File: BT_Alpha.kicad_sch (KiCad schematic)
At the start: 97 parts, among them J1 61300511121, J2 S6B-PH-K-S, J3 S6B-PH-K-S, J4 Boxed_Header_02x03_SMT, K1 AGQ200A12Z, M1 Mounting_Hole_2.7mm_Unplated, M2 Mounting_Hole_2.7mm_Unplated, M3 Mounting_Hole_2.7mm_Unplated, Q1 BSS123, Q2 BSS123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

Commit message: started iterating to rev. B
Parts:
- removed C16: 100nF, NRD_CAP:C_0603, symbol NRD_C_0603:CL10B104KB8NNNC
- removed C8, C9: 3.3nF, NRD_CAP:C_0603, symbol NRD_C_0603:CL10B332MB8NNNC
- removed J1: 61300511121, NRD_PinHeader:61300511121, symbol NRD_PinHeader:61300511121
- removed R1, R4: 470R, NRD_RES:R_0603, symbol NRD_R_0603:RC0603FR-07470RL
- removed R10, R11, R12, R22, R23, R24, R25, R27, R28, R29, R30, R9: 1M, NRD_RES:R_0603, symbol NRD_R_0603:RC0603FR-071ML
- removed R13, R14, R15: 0R, NRD_RES:R_0603, symbol NRD_R_0603:RC0603FR-070RL
- removed R16, R21, R26: 10K, NRD_RES:R_0603, symbol NRD_R_0603:RC0603FR-0710KL
- removed R33: 10K, NRD_R_Var:TC33X-2, symbol NRD_R_Var:TC33X-2-103E
- removed U3: TLV4888DR, NRD_IC_OPAMP:TLV4888DR, symbol NRD_IC_OPAMP:TLV4888DR
- removed Y1: XO32, Oscillator:Oscillator_SMD_EuroQuartz_XO32-4Pin_3.2x2.5mm, symbol Oscillator:XO32
- added C22, C37: 10uF, NRD_CAP:C_0805, symbol NRD_C_0805:CL21B106KOQNNNG
- added R41, R42, R43, R44: 10K, NRD_RES:R_0603, symbol NRD_R_0603:RC0603FR-0710KL
- added U3: TLV2888DR, NRD_IC_OPAMP:TLV2888DR, symbol NRD_IC_OPAMP:TLV2888DR
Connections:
- net SCK is gone; now on net ESP_IO0: U1.12 (SCK)
- net +12V: now also K1.8; no longer K1.1
- net GND: now also R41.1, R42.1, U3.4 (V-)
- net OUT_L: now also C22.2
- net OUT_R: now also C37.2
- net at C15.2, TP3.1: now also U3.6 (-), U3.7
- net at C14.2, TP2.1: now also U3.1, U3.2 (-)
- net at D1.A, Q1.3 (D): now also K1.1; no longer K1.8
- net +6V_FLT: now reaches C27.1, C36.1, L2.2
- net +6V_FLT: now also R43.2, R44.2, U3.8 (V+)
- net MCLK: no longer names the net of U2.27 (IO16)
- new net: C37.1, R41.2, R43.1, U3.5 (+)
- new net: C22.1, R42.2, R44.1, U3.3 (+)
- no-connect marks 27 -> 25
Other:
- note added: "(MCLK)"
- note added: "TLV2888"
- note removed: "(CLK_OUT1)"
- note removed: "(from MCU)"
- note removed: "(to DAC)"
- note removed: "AppNote uses 2.2nF for reconstruction filter. 2.2nF only as C0G in databbase -> 3.3nF C7R acceptable as well -> fg = 102.6kHz (instead of 153.9kHz)"
- note removed: "DAC Clock"
- note removed: "credits amplifier: https://electronics.stackexchange.com/questions/450609/op-amp-circuit-to-control-gain-of-two-analog-channels-with-one-single-section-po"
- moved on the sheet: C14, C15, D1, K1, Q1, Q2, R34, R8, TP2, TP3

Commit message: wip
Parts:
- removed TP1, TP2, TP3: 5001, NRD_MISC:500x, symbol NRD_MISC:5001
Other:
- moved on the sheet: M1, M2, M3

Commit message: added credits
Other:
- moved on the sheet: C14, C15, C34, Q2, R34, R39, R8

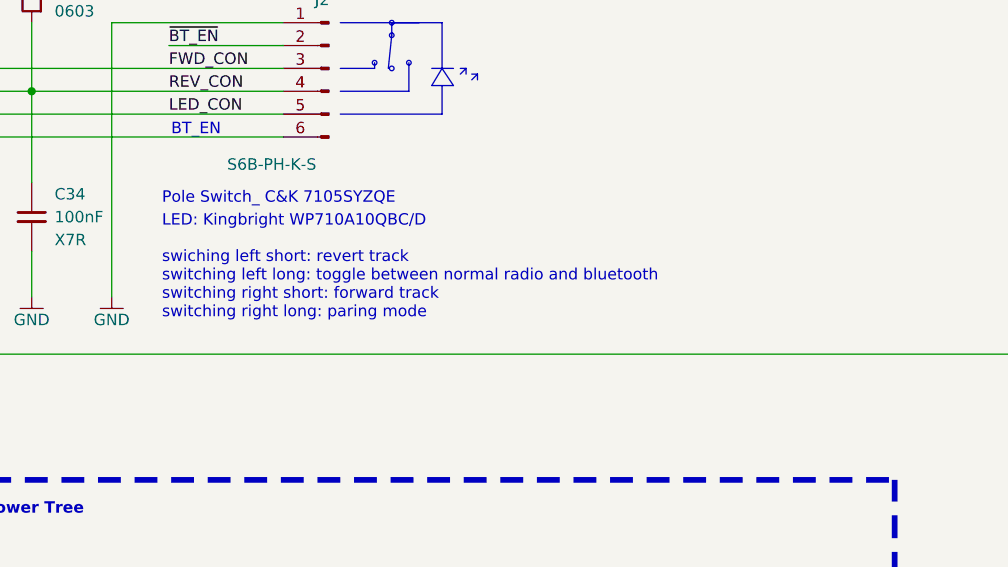
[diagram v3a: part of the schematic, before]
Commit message: fixed state machine
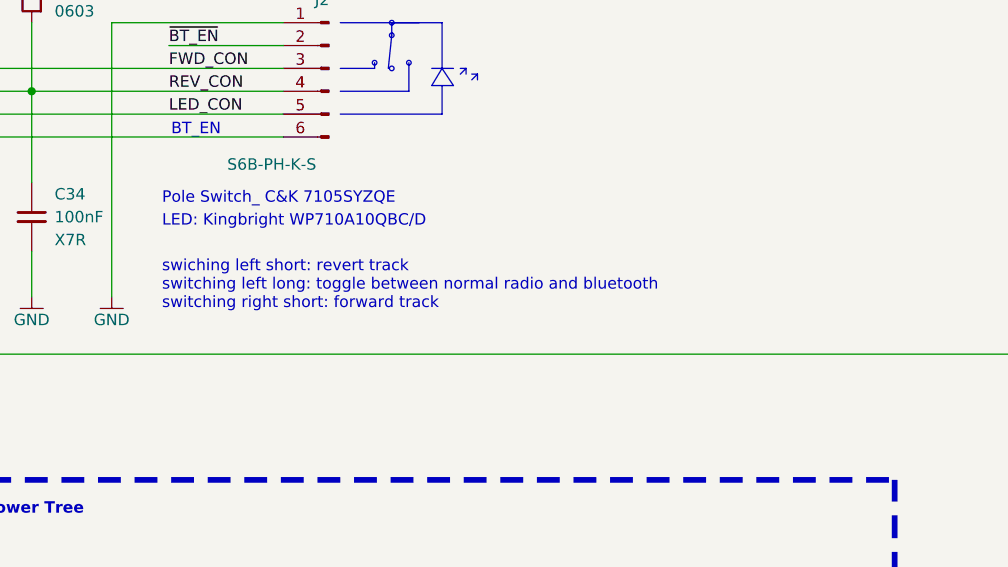
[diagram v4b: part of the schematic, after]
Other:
- note added: "swiching left short: revert track switching left long: toggle between normal radio and bluetooth switching right short: forward track"
- note removed: "swiching left short: revert track switching left long: toggle between normal radio and bluetooth switching right short: forward track switching right long: paring mode"
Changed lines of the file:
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@@
 		)
 	)
-	(text "swiching left short: revert track\nswitching left long: toggle between normal radio and bluetooth\nswitching right short: forward track\nswitching right long: paring mode"
+	(text "swiching left short: revert track\nswitching left long: toggle between normal radio and bluetooth\nswitching right short: forward track"
 		(exclude_from_sim no)
 		(at 218.948 140.97 0)
